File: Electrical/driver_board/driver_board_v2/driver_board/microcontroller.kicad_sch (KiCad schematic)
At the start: 24 parts, among them J1 USB_C_Receptacle_USB2.0_14P, J2 Conn_01x04_Pin, SW1 SW_SPDT, SW2 SW_Push, U1 STM32F446RETx, Y1 8Mhz

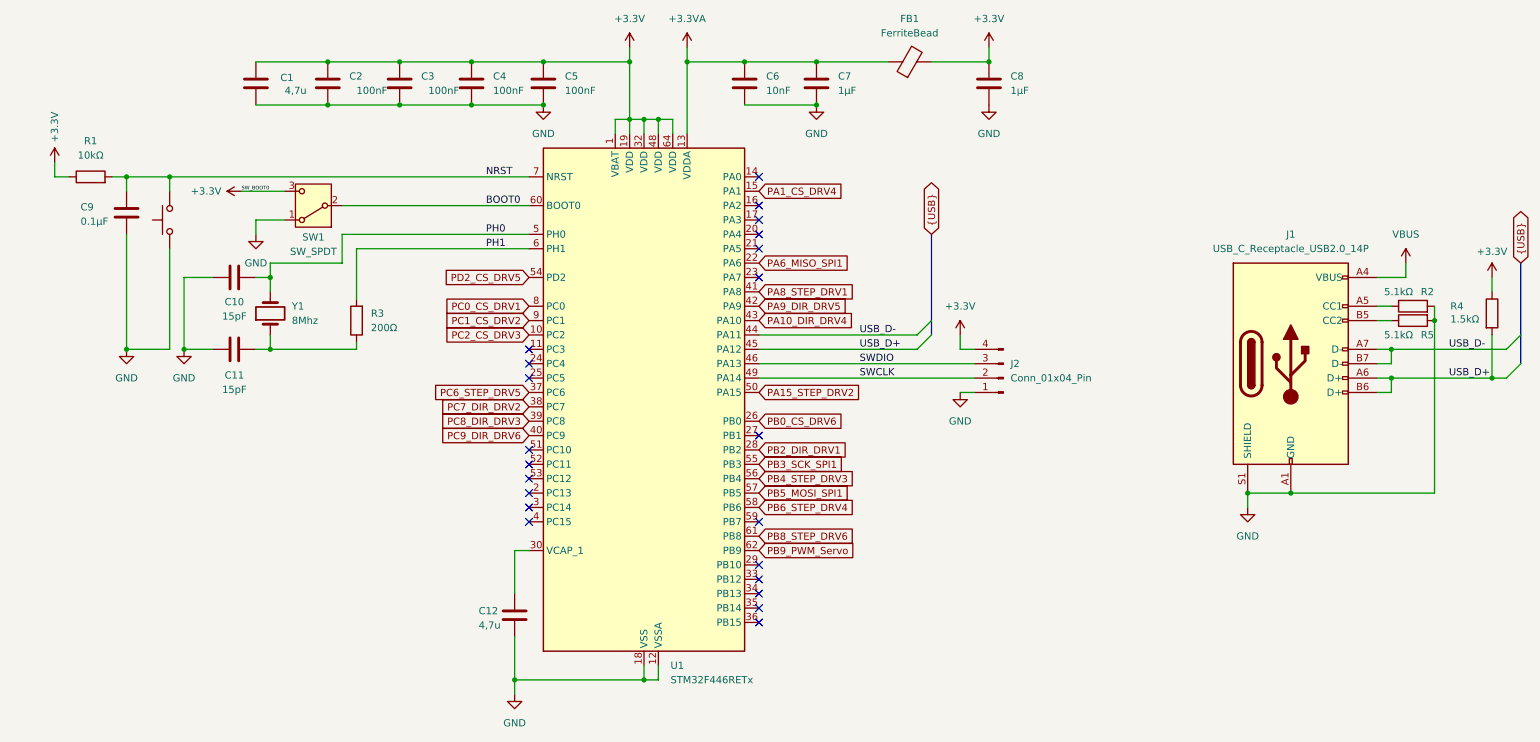
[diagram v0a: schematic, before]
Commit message: Value assignment and protection for driver board
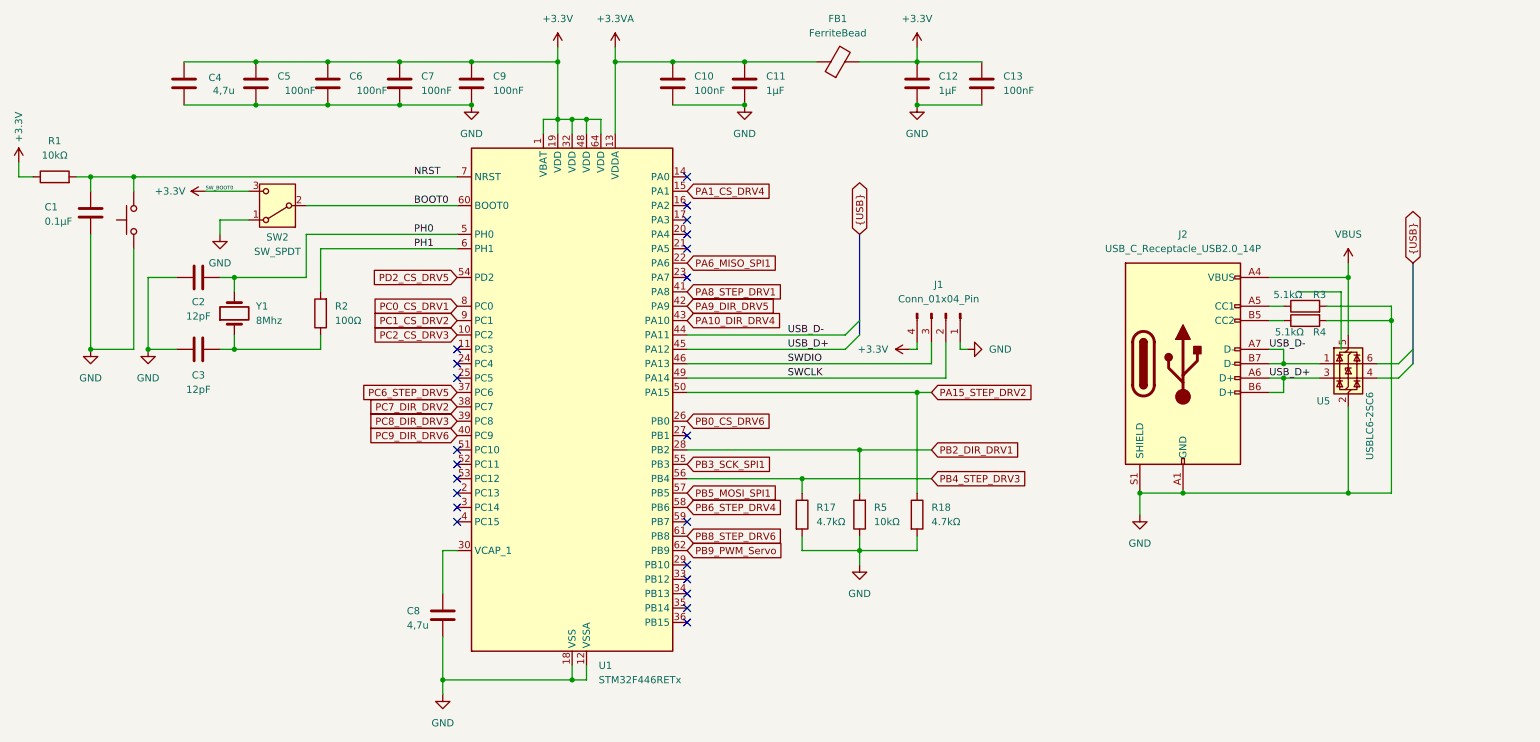
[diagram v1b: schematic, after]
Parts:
- removed R4: 1.5kΩ, symbol Device:R
- added C13: 100nF, symbol Device:C
- added R17, R18: 4.7kΩ, symbol Device:R
- added R5: 10kΩ, symbol Device:R
- added U5: USBLC6-2SC6, Package_TO_SOT_SMD:SOT-23-6, symbol Power_Protection:USBLC6-2SC6
- C10: renamed from C6; value 10nF -> 100nF
- C2: renamed from C10; value 15pF -> 12pF
- C3: renamed from C11; value 15pF -> 12pF
- R2: renamed from R3; value 200Ω -> 100Ω
- renumbered C9 to C1, C7 to C11, C8 to C12, C1 to C4, C2 to C5, C3 to C6, C4 to C7, C12 to C8, C5 to C9, J2 to J1, J1 to J2, R2 to R3, R5 to R4, SW2 to SW1, SW1 to SW2
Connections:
- net +3.3V: now also C13.1
- net GND: now also C13.2, R17.2, R18.2, R5.1, U5.2 (GND)
- net PA15_STEP_DRV2: now also R18.1
- net PB2_DIR_DRV1: now also R5.2
- net PB4_STEP_DRV3: now also R17.1
- net USB_D+: now also U5.3 (I/O2)
- net USB_D-: now also U5.1 (I/O1)
- net VBUS: now also U5.5 (VBUS)
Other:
- moved on the sheet: C1, C10, C11, C12, C2, C3, C4, C5, C6, C7, C8, C9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
